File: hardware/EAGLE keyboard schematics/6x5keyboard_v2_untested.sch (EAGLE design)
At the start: 71 parts

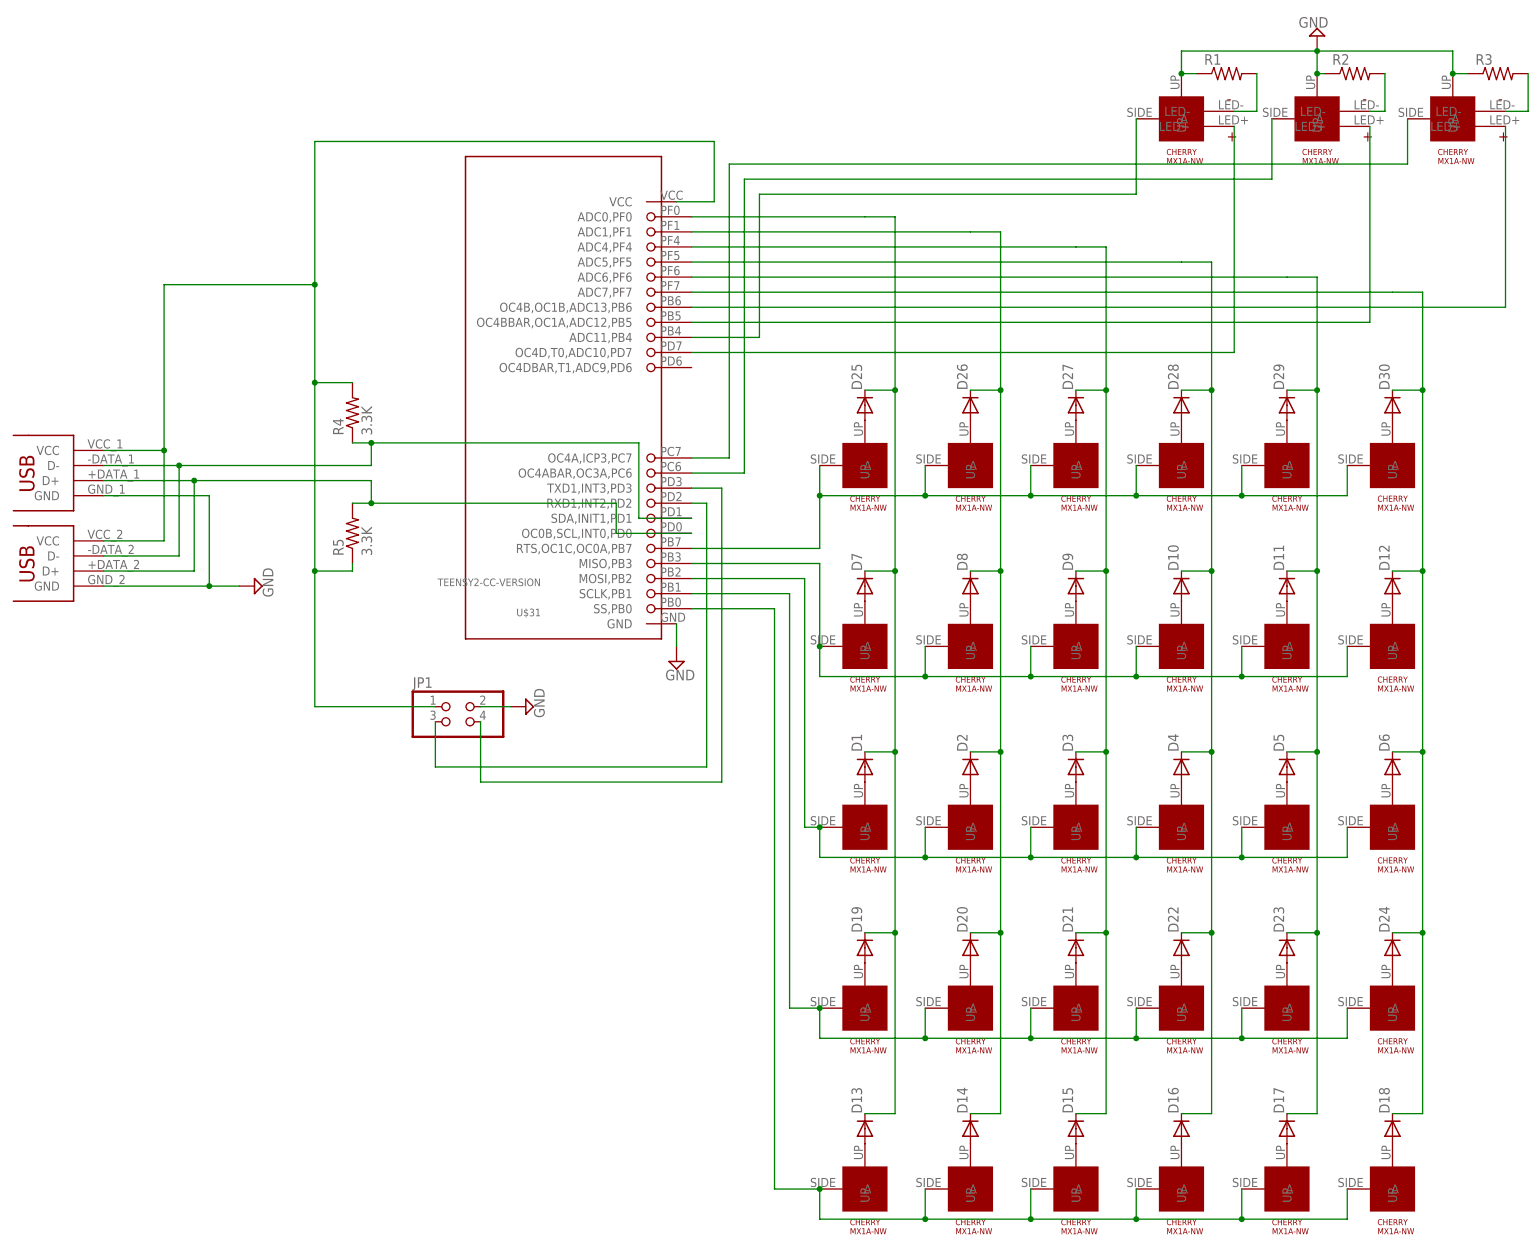
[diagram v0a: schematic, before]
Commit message: Corrected the ERC warnings.
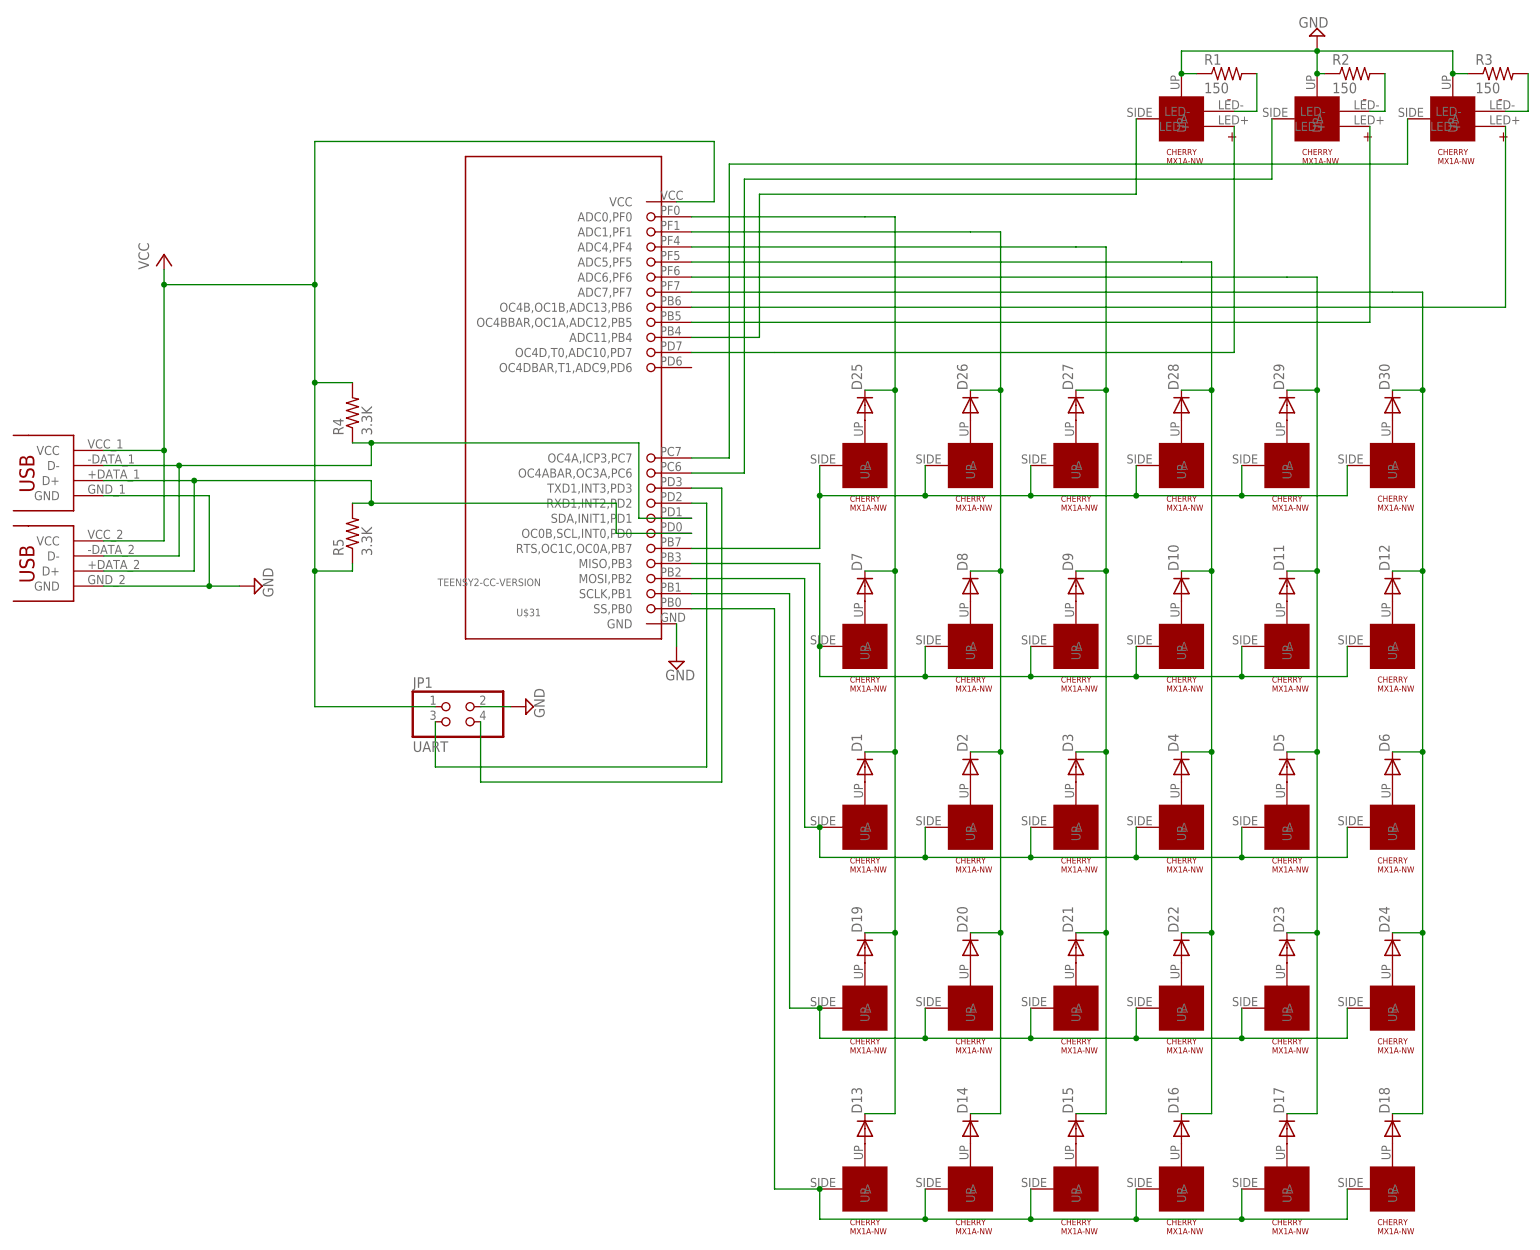
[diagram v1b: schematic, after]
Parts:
- JP1: value (none) -> UART
- R1, R2, R3: value (none) -> 150
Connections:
- net N$51 renamed VCC
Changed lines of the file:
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@@
 <setting verticaltext="up"/>
 </settings>
-<grid distance="0.05" unitdist="inch" unit="inch" style="lines" multiple="1" display="no" altdistance="0.025" altunitdist="inch" altunit="inch"/>
+<grid distance="0.1" unitdist="inch" unit="inch" style="lines" multiple="1" display="no" altdistance="0.01" altunitdist="inch" altunit="inch"/>
 <layers>
 <layer number="1" name="Top" color="4" fill="1" visible="no" active="no"/>
@@
 <part name="U$34" library="my_parts" deviceset="CHERRY-MX1A-E1NW-LED" device=""/>
 <part name="SUPPLY1" library="supply2" deviceset="GND" device=""/>
-<part name="R1" library="rcl" deviceset="R-US_" device="0207/10"/>
-<part name="R2" library="rcl" deviceset="R-US_" device="0207/10"/>
-<part name="R3" library="rcl" deviceset="R-US_" device="0207/10"/>
+<part name="R1" library="rcl" deviceset="R-US_" device="0207/10" value="150"/>
+<part name="R2" library="rcl" deviceset="R-US_" device="0207/10" value="150"/>
+<part name="R3" library="rcl" deviceset="R-US_" device="0207/10" value="150"/>
 <part name="SUPPLY2" library="supply2" deviceset="GND" device=""/>
 <part name="R4" library="resistor" deviceset="R-US_" device="0207/10" value="3.3K"/>
 <part name="R5" library="resistor" deviceset="R-US_" device="0207/10" value="3.3K"/>
-<part name="JP1" library="pinhead" deviceset="PINHD-2X2" device=""/>
+<part name="JP1" library="pinhead" deviceset="PINHD-2X2" device="" value="UART"/>
 <part name="SUPPLY4" library="supply2" deviceset="GND" device=""/>
 <part name="U$35" library="my_parts" deviceset="DUAL-USB-A" device=""/>
 <part name="SUPPLY5" library="supply2" deviceset="GND" device=""/>
+<part name="P+1" library="supply1" deviceset="VCC" device=""/>
 </parts>
 <sheets>
@@
 <instance part="U$35" gate="G$2" x="-96.52" y="96.52"/>
 <instance part="SUPPLY5" gate="GND" x="-71.12" y="93.98" rot="R90"/>
+<instance part="P+1" gate="VCC" x="-86.36" y="149.86"/>
 </instances>
 <busses>
@@
 </segment>
 </net>
-<net name="N$51" class="0">
+<net name="VCC" class="0">
 <segment>
 <pinref part="U$35" gate="G$1" pin="VCC"/>
@@
 <wire x1="-54.61" y1="96.52" x2="-54.61" y2="97.79" width="0.1524" layer="91"/>
 <junction x="-60.96" y="96.52"/>
-</segment>
-</net>
+<pinref part="P+1" gate="VCC" pin="VCC"/>
+<wire x1="-86.36" y1="147.32" x2="-86.36" y2="144.78" width="0.1524" layer="91"/>
+<junction x="-86.36" y="144.78"/>
+</segment>
+</net>
